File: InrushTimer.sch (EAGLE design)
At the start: 78 parts, among them IC2 TLC272D, IC3 4076N, IC5 555, IC6 555, Q2 TIP41C

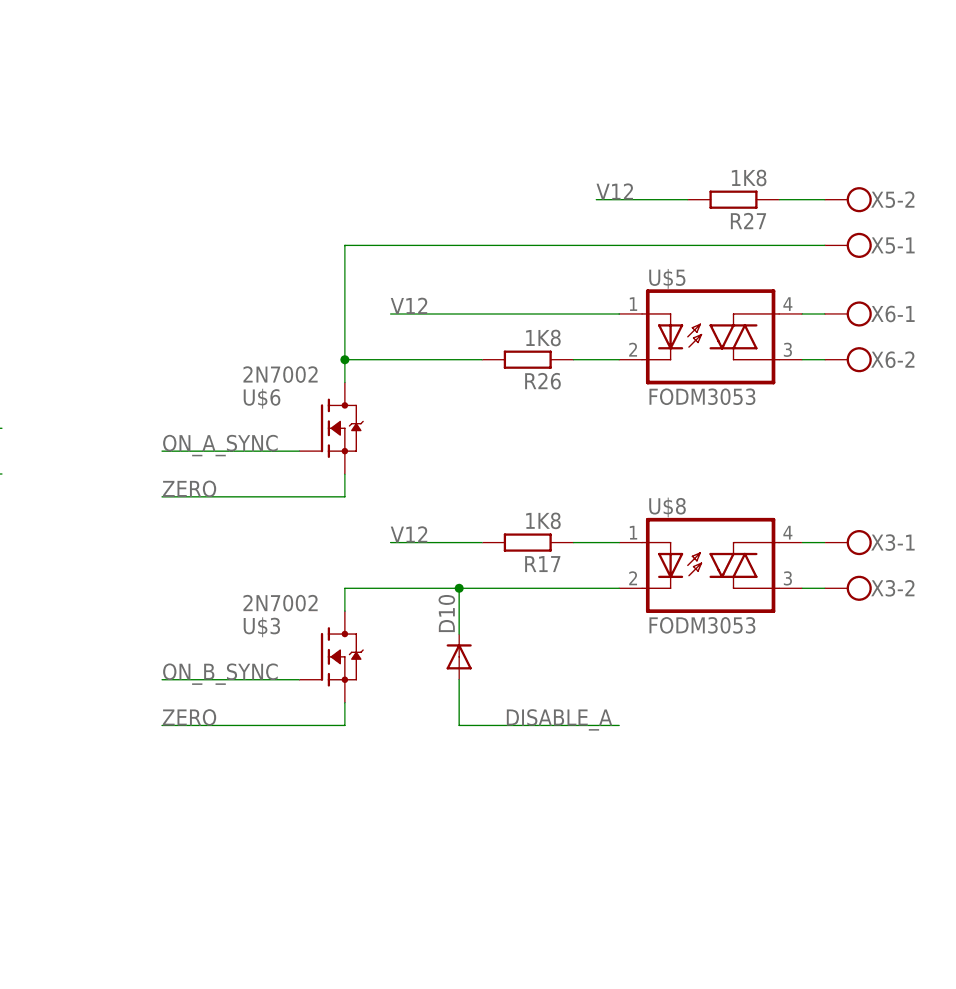
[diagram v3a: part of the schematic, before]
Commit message: Updated schematics and board to address error in aux output assignment.
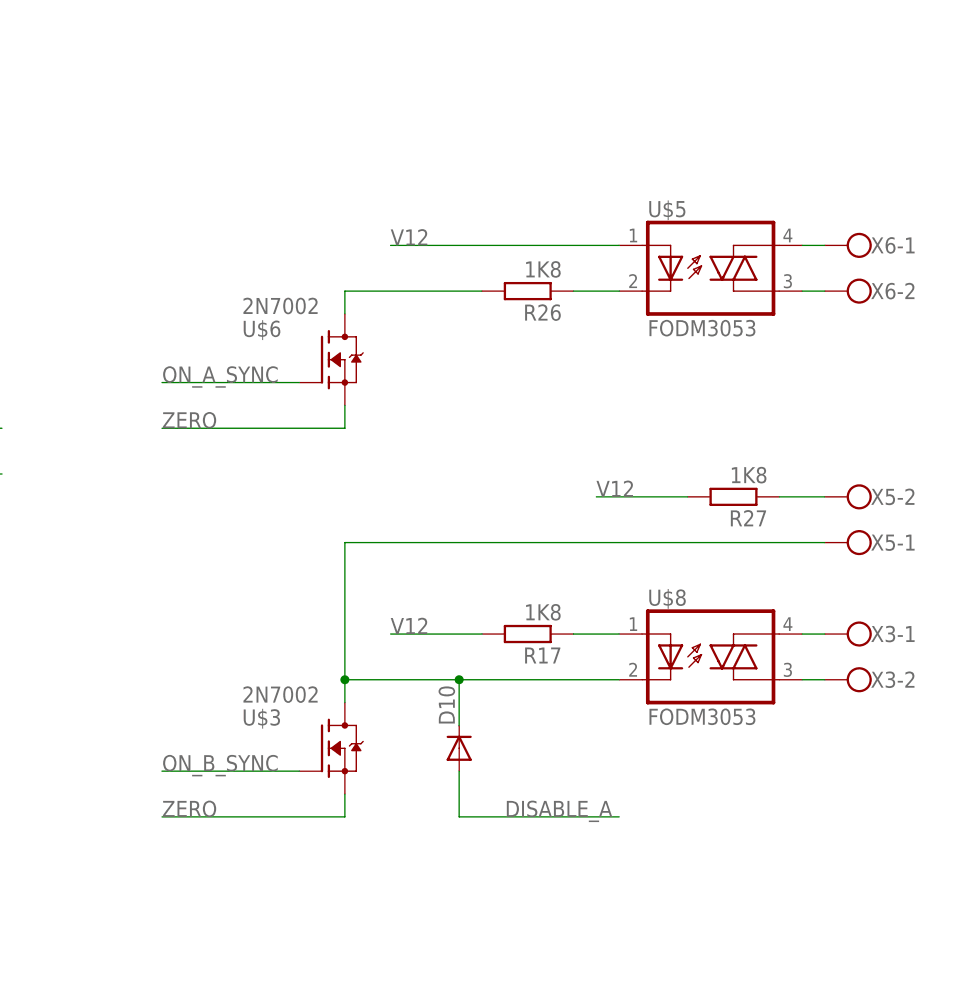
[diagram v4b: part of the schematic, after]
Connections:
- removed net N$33: D10.C, U$3.D, U$8.C
- new net N$31: R26.2, U$6.D
- net N$6: now also D10.C, U$3.D, U$8.C; no longer R26.2, U$6.D
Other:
- moved on the sheet: D10, R17, R26, R27, U$3, U$5, U$6, U$8, X3-1, X3-2, X5-1, X5-2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

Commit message: Committing changes to circuit to remove a time and put the optoisolators into series.
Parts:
- removed C17: 10nF, rcl:C-EU050-024X044
- removed C7: 1uF, rcl:C-EUC1206K
- removed C8: 100nF, rcl:C-EU050-024X044
- removed IC5: 555, linear:555
- removed R16: 220K, pot:TRIM_EU-CA6H
- removed R18: 51K, rcl:R-EU_0207/7
- removed R22: 51K, rcl:R-EU_0207/5V
- removed R23: 100R, rcl:R-EU_0207/7
- removed R27: 1K8, rcl:R-EU_R0805
- removed R5: 100K, rcl:R-EU_0207/2V
- removed U$1, U$2: 2N7002, transistor-fet:2N7002
- added U$9: FODM3053, SHoleLib:FODM3053
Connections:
- removed net N$12 (its old number): R27.1, X5-2.KL
- removed net N$13: C16.1, D1.C, R14.2, U$13.G, U$4.VOUT
- removed net N$25: R16.E, R5.1
- removed net N$35: C17.1, IC5.CV
- removed net N$4 (its old number): C7.2, IC5.DIS, IC5.THR, R16.A, R16.S
- removed net N$47: IC5.Q, R23.2
- removed net ON_A: IC3A.D2, R22.2, U$1.D
- new net N$15: R17.2, U$8.A
- new net N$17: R17.1, U$9.C
- net N$20: now also U$9.A2, X5-2.KL; no longer R17.1, U$8.A
- net N$21: now also U$9.A1, X5-1.KL; no longer R23.1, U$1.G
- net N$6: no longer X5-1.KL
- net RESET: no longer U$2.G
- net RESET_N: now also C16.1, D1.C, R14.2, U$13.G, U$4.VOUT; no longer IC5.R, IC5.TR, R18.1, U$2.D
- net V12: now also IC3A.D2, U$9.A; no longer C8.1, IC5.V+, R17.2, R18.2, R22.1, R27.2, R5.2
- net ZERO: no longer C17.2, C7.1, C8.2, IC5.GND, U$1.S, U$2.S
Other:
- moved on the sheet: D10, R15, R17, U$13, U$3, U$8, X3-1, X3-2, X5-1, X5-2

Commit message: Updated model and board with circuit and component values.
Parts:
- removed R9: 37K4, rcl:R-EU_0207/2V
- added C17, C8: 10nF, rcl:C-EU050-024X044
- added C7: 1nF, rcl:C-EUC0805K
- added R2: 10K, rcl:R-EU_0207/2V
- added T2: (no value), transistor:MMBTA42LT1-NPN-SOT23-BEC
- C6: value 1uF -> 2.2uF
- D7: value (none) -> STTH110
- R17, R26: value 1K8 -> 1K
- R19: value 22K -> 10K
- R7: value 37K4 -> 27K
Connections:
- removed net N$30: C14.1, D12.C, R7.2, R9.2
- new net N$13: R2.2, T2.E, U$4.VDD
- net N$14: now also C14.1, D12.C, R7.2, T2.B; no longer R9.1, U$4.VDD
- net N$26: now also C17.1
- net N$34: now also C8.1
- net N$7: now also C7.2
- net N$9: now also C7.1
- net RECT: now also T2.C
- net ZERO: now also C17.2, C8.2, R2.1
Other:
- moved on the sheet: C14, C16, D1, D12, R14, R15, R19, R7, U$13

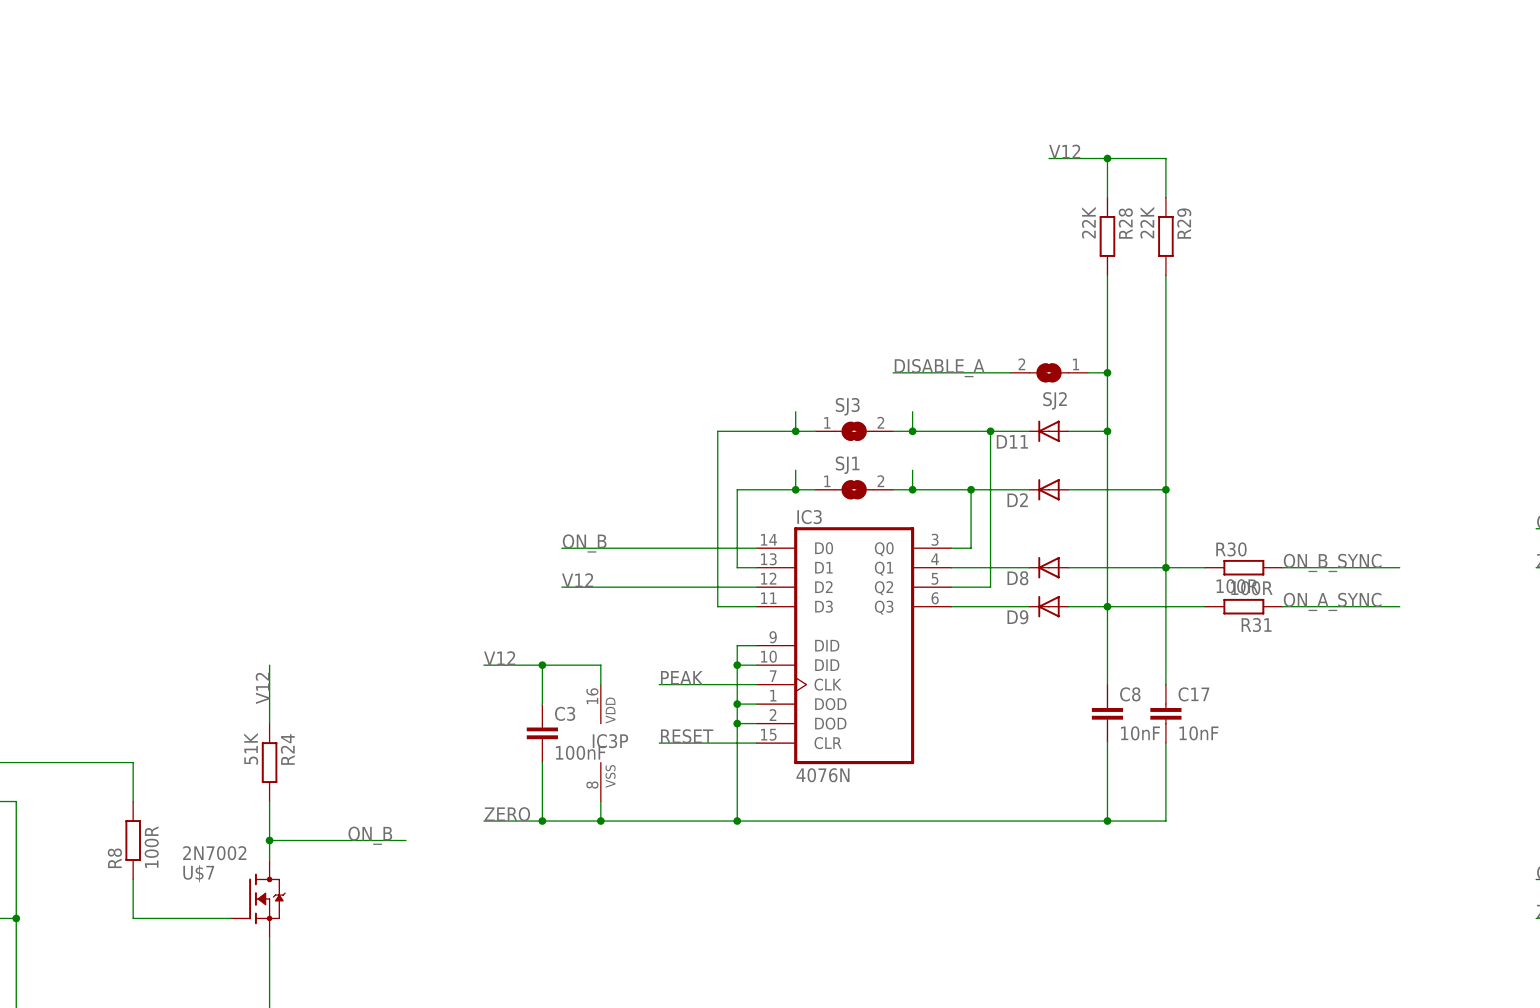
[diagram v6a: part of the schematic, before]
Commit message: Changed gate resistors and checked component values.
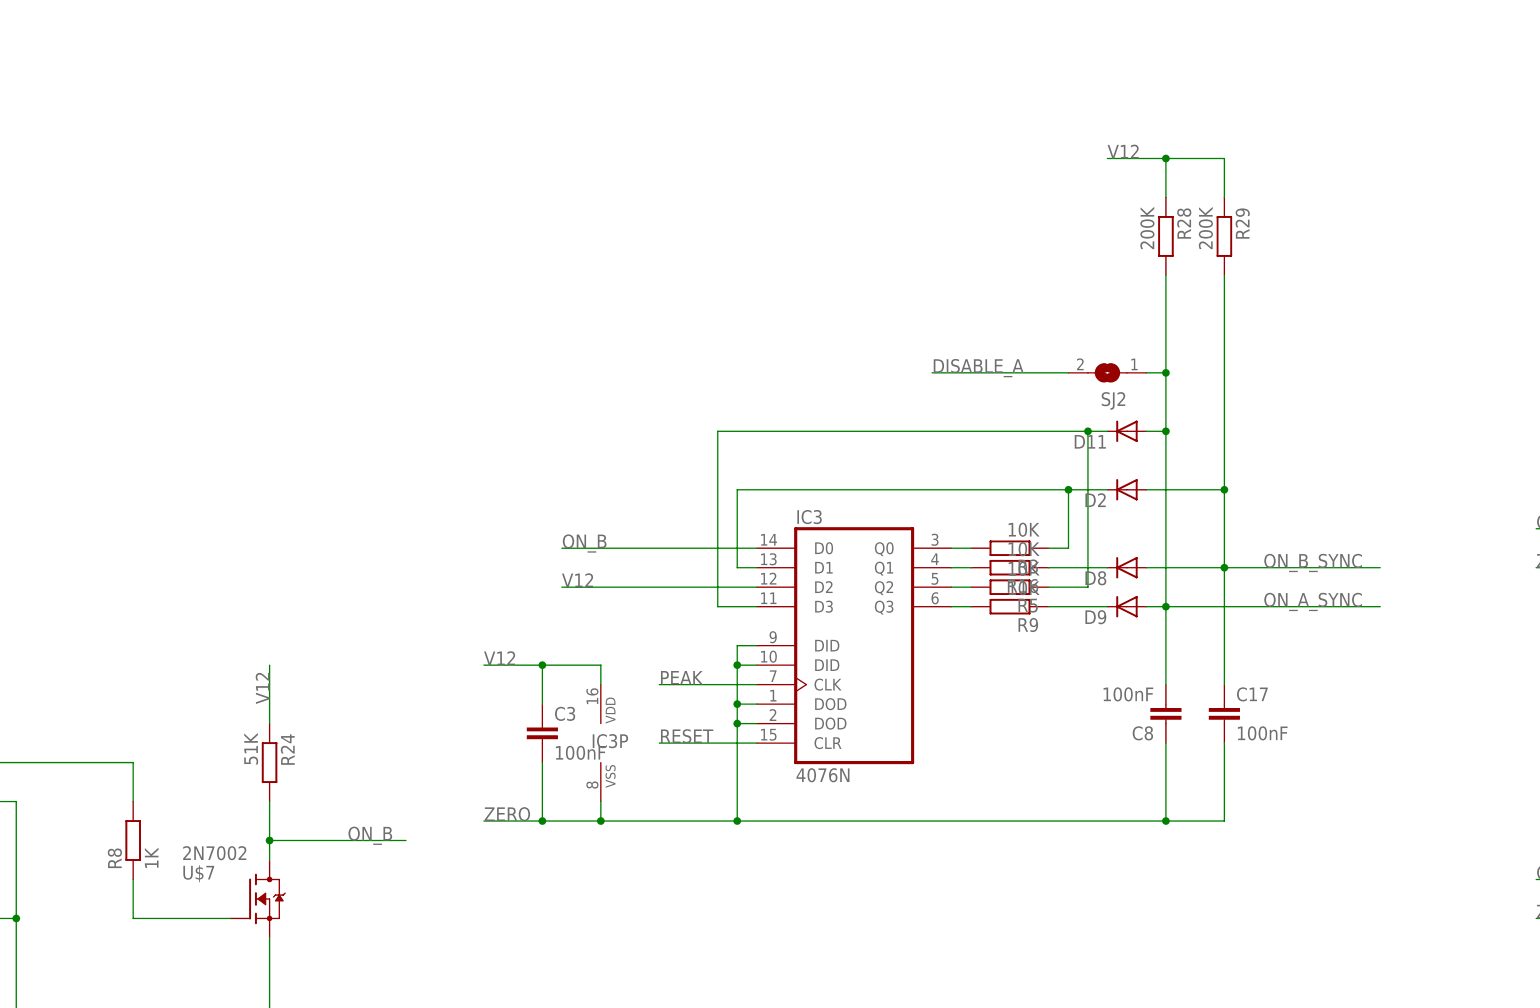
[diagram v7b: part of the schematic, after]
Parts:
- removed R30: 100R, rcl:R-EU_0207/2V
- removed R31: 100R, rcl:R-EU_0207/5V
- removed SJ1, SJ3: (no value), jumper:SJ
- added R16, R3, R5, R9: 10K, rcl:R-EU_0207/2V
- C17, C8: value 10nF -> 100nF
- R28, R29: value 22K -> 200K
- R8: value 100R -> 1K
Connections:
- removed net N$23: D2.C, IC3A.Q0, SJ1.2
- removed net N$26: C17.1, D2.A, D8.A, R29.2, R30.1
- removed net N$34: C8.1, D11.A, D9.A, R28.2, R31.2, SJ2.1
- new net N$25: IC3A.Q1, R16.2
- new net N$30: D8.C, R16.1
- new net N$32: IC3A.Q0, R3.2
- net N$16: now also D2.C, R3.1; no longer SJ1.1
- net N$19: now also R5.2; no longer D11.C, SJ3.2
- net N$22: now also D11.C, R5.1; no longer SJ3.1
- net N$24: now also D9.C, R9.1; no longer D8.C, IC3A.Q1
- net N$3: now also R9.2; no longer D9.C
- net ON_A_SYNC: now also C8.2, D11.A, D9.A, R28.2, SJ2.1; no longer R31.1
- net ON_B_SYNC: now also C17.1, D2.A, D8.A, R29.2; no longer R30.2
- net ZERO: now also C8.1; no longer C8.2
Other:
- moved on the sheet: C17, C8, D11, D2, D8, D9, R28, R29, SJ2
